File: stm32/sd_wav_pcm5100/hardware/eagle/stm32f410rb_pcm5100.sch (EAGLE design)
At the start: 33 parts, among them IC1 STM32F410_8_B_LQFP64, U5 PCM5100

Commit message: added dirtypcb gerbers
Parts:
- C28, C29: value 2200pF -> 2.2nF
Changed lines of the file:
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@@
 <grid distance="0.1" unitdist="inch" unit="inch" style="lines" multiple="1" display="no" altdistance="0.01" altunitdist="inch" altunit="inch"/>
 <layers>
-<layer number="1" name="Top" color="4" fill="1" visible="yes" active="no"/>
-<layer number="2" name="Route2" color="1" fill="3" visible="yes" active="no"/>
-<layer number="3" name="Route3" color="4" fill="3" visible="yes" active="no"/>
-<layer number="4" name="Route4" color="1" fill="4" visible="yes" active="no"/>
-<layer number="5" name="Route5" color="4" fill="4" visible="yes" active="no"/>
-<layer number="6" name="Route6" color="1" fill="8" visible="yes" active="no"/>
-<layer number="7" name="Route7" color="4" fill="8" visible="yes" active="no"/>
-<layer number="8" name="Route8" color="1" fill="2" visible="yes" active="no"/>
-<layer number="9" name="Route9" color="4" fill="2" visible="yes" active="no"/>
-<layer number="10" name="Route10" color="1" fill="7" visible="yes" active="no"/>
-<layer number="11" name="Route11" color="4" fill="7" visible="yes" active="no"/>
-<layer number="12" name="Route12" color="1" fill="5" visible="yes" active="no"/>
-<layer number="13" name="Route13" color="4" fill="5" visible="yes" active="no"/>
-<layer number="14" name="Route14" color="1" fill="6" visible="yes" active="no"/>
-<layer number="15" name="Route15" color="4" fill="6" visible="yes" active="no"/>
-<layer number="16" name="Bottom" color="1" fill="1" visible="yes" active="no"/>
-<layer number="17" name="Pads" color="2" fill="1" visible="yes" active="no"/>
-<layer number="18" name="Vias" color="2" fill="1" visible="yes" active="no"/>
-<layer number="19" name="Unrouted" color="6" fill="1" visible="yes" active="no"/>
-<layer number="20" name="Dimension" color="15" fill="1" visible="yes" active="no"/>
-<layer number="21" name="tPlace" color="7" fill="1" visible="yes" active="no"/>
-<layer number="22" name="bPlace" color="7" fill="1" visible="yes" active="no"/>
-<layer number="23" name="tOrigins" color="15" fill="1" visible="yes" active="no"/>
-<layer number="24" name="bOrigins" color="15" fill="1" visible="yes" active="no"/>
-<layer number="25" name="tNames" color="7" fill="1" visible="yes" active="no"/>
-<layer number="26" name="bNames" color="7" fill="1" visible="yes" active="no"/>
-<layer number="27" name="tValues" color="7" fill="1" visible="yes" active="no"/>
-<layer number="28" name="bValues" color="7" fill="1" visible="yes" active="no"/>
+<layer number="1" name="Top" color="4" fill="1" visible="no" active="no"/>
+<layer number="2" name="Route2" color="1" fill="3" visible="no" active="no"/>
+<layer number="3" name="Route3" color="4" fill="3" visible="no" active="no"/>
+<layer number="4" name="Route4" color="1" fill="4" visible="no" active="no"/>
+<layer number="5" name="Route5" color="4" fill="4" visible="no" active="no"/>
+<layer number="6" name="Route6" color="1" fill="8" visible="no" active="no"/>
+<layer number="7" name="Route7" color="4" fill="8" visible="no" active="no"/>
+<layer number="8" name="Route8" color="1" fill="2" visible="no" active="no"/>
+<layer number="9" name="Route9" color="4" fill="2" visible="no" active="no"/>
+<layer number="10" name="Route10" color="1" fill="7" visible="no" active="no"/>
+<layer number="11" name="Route11" color="4" fill="7" visible="no" active="no"/>
+<layer number="12" name="Route12" color="1" fill="5" visible="no" active="no"/>
+<layer number="13" name="Route13" color="4" fill="5" visible="no" active="no"/>
+<layer number="14" name="Route14" color="1" fill="6" visible="no" active="no"/>
+<layer number="15" name="Route15" color="4" fill="6" visible="no" active="no"/>
+<layer number="16" name="Bottom" color="1" fill="1" visible="no" active="no"/>
+<layer number="17" name="Pads" color="2" fill="1" visible="no" active="no"/>
+<layer number="18" name="Vias" color="2" fill="1" visible="no" active="no"/>
+<layer number="19" name="Unrouted" color="6" fill="1" visible="no" active="no"/>
+<layer number="20" name="Dimension" color="15" fill="1" visible="no" active="no"/>
+<layer number="21" name="tPlace" color="7" fill="1" visible="no" active="no"/>
+<layer number="22" name="bPlace" color="7" fill="1" visible="no" active="no"/>
+<layer number="23" name="tOrigins" color="15" fill="1" visible="no" active="no"/>
+<layer number="24" name="bOrigins" color="15" fill="1" visible="no" active="no"/>
+<layer number="25" name="tNames" color="7" fill="1" visible="no" active="no"/>
+<layer number="26" name="bNames" color="7" fill="1" visible="no" active="no"/>
+<layer number="27" name="tValues" color="7" fill="1" visible="no" active="no"/>
+<layer number="28" name="bValues" color="7" fill="1" visible="no" active="no"/>
 <layer number="29" name="tStop" color="7" fill="3" visible="no" active="no"/>
 <layer number="30" name="bStop" color="7" fill="6" visible="no" active="no"/>
@@
 <layer number="35" name="tGlue" color="7" fill="4" visible="no" active="no"/>
 <layer number="36" name="bGlue" color="7" fill="5" visible="no" active="no"/>
-<layer number="37" name="tTest" color="7" fill="1" visible="yes" active="no"/>
-<layer number="38" name="bTest" color="7" fill="1" visible="yes" active="no"/>
+<layer number="37" name="tTest" color="7" fill="1" visible="no" active="no"/>
+<layer number="38" name="bTest" color="7" fill="1" visible="no" active="no"/>
 <layer number="39" name="tKeepout" color="4" fill="11" visible="no" active="no"/>
 <layer number="40" name="bKeepout" color="1" fill="11" visible="no" active="no"/>
@@
 <layer number="44" name="Drills" color="7" fill="1" visible="no" active="no"/>
 <layer number="45" name="Holes" color="7" fill="1" visible="no" active="no"/>
-<layer number="46" name="Milling" color="3" fill="1" visible="yes" active="no"/>
-<layer number="47" name="Measures" color="7" fill="1" visible="yes" active="no"/>
-<layer number="48" name="Document" color="7" fill="1" visible="yes" active="no"/>
-<layer number="49" name="Reference" color="7" fill="1" visible="yes" active="no"/>
-<layer number="50" name="dxf" color="7" fill="1" visible="yes" active="no"/>
-<layer number="51" name="tDocu" color="7" fill="1" visible="yes" active="no"/>
-<layer number="52" name="bDocu" color="7" fill="1" visible="yes" active="no"/>
-<layer number="53" name="tGND_GNDA" color="7" fill="9" visible="yes" active="no"/>
-<layer number="54" name="bGND_GNDA" color="1" fill="9" visible="yes" active="no"/>
-<layer number="56" name="wert" color="7" fill="1" visible="yes" active="no"/>
-<layer number="57" name="tCAD" color="7" fill="1" visible="yes" active="no"/>
-<layer number="59" name="tCarbon" color="7" fill="1" visible="yes" active="no"/>
-<layer number="60" name="bCarbon" color="7" fill="1" visible="yes" active="no"/>
+<layer number="46" name="Milling" color="3" fill="1" visible="no" active="no"/>
+<layer number="47" name="Measures" color="7" fill="1" visible="no" active="no"/>
+<layer number="48" name="Document" color="7" fill="1" visible="no" active="no"/>
+<layer number="49" name="Reference" color="7" fill="1" visible="no" active="no"/>
+<layer number="50" name="dxf" color="7" fill="1" visible="no" active="no"/>
+<layer number="51" name="tDocu" color="7" fill="1" visible="no" active="no"/>
+<layer number="52" name="bDocu" color="7" fill="1" visible="no" active="no"/>
+<layer number="53" name="tGND_GNDA" color="7" fill="9" visible="no" active="no"/>
+<layer number="54" name="bGND_GNDA" color="1" fill="9" visible="no" active="no"/>
+<layer number="56" name="wert" color="7" fill="1" visible="no" active="no"/>
+<layer number="57" name="tCAD" color="7" fill="1" visible="no" active="no"/>
+<layer number="59" name="tCarbon" color="7" fill="1" visible="no" active="no"/>
+<layer number="60" name="bCarbon" color="7" fill="1" visible="no" active="no"/>
 <layer number="90" name="Modules" color="5" fill="1" visible="yes" active="yes"/>
 <layer number="91" name="Nets" color="2" fill="1" visible="yes" active="yes"/>
@@
 <part name="C26" library="SparkFun-Passives" deviceset="CAP" device="0805" value="0.1uF"/>
 <part name="C27" library="SparkFun-Passives" deviceset="CAP" device="0805" value="10uF"/>
-<part name="C28" library="SparkFun-Passives" deviceset="CAP" device="0805" value="2200pF"/>
-<part name="C29" library="SparkFun-Passives" deviceset="CAP" device="0805" value="2200pF"/>
+<part name="C28" library="SparkFun-Passives" deviceset="CAP" device="0805" value="2.2nF"/>
+<part name="C29" library="SparkFun-Passives" deviceset="CAP" device="0805" value="2.2nF"/>
 <part name="R6" library="SparkFun-Passives" deviceset="RESISTOR" device="0805-RES" value="470"/>
 <part name="R7" library="SparkFun-Passives" deviceset="RESISTOR" device="0805-RES" value="470"/>

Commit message: refactored pcb
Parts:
- JP2: value M023.5MM -> Vsupply - 3.3Vcc
- MMC1: value MICROSD_AMPHENOL -> Amphenol
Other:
- note added: "TT"
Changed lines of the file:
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@@
 <setting verticaltext="up"/>
 </settings>
-<grid distance="0.1" unitdist="inch" unit="inch" style="lines" multiple="1" display="no" altdistance="0.01" altunitdist="inch" altunit="inch"/>
+<grid distance="0.01" unitdist="inch" unit="inch" style="dots" multiple="1" display="yes" altdistance="0.01" altunitdist="inch" altunit="inch"/>
 <layers>
 <layer number="1" name="Top" color="4" fill="1" visible="no" active="no"/>
@@
 <part name="C9" library="SparkFun-Passives" deviceset="CAP" device="0805" value="0.1uF"/>
 <part name="GND14" library="supply1" deviceset="GND" device=""/>
-<part name="MMC1" library="microsd_amphenol" deviceset="MICROSD_AMPHENOL" device=""/>
+<part name="MMC1" library="microsd_amphenol" deviceset="MICROSD_AMPHENOL" device="" value="Amphenol"/>
 <part name="P+6" library="supply1" deviceset="VCC" device="" value="+3V3"/>
 <part name="P+1" library="supply1" deviceset="VCC" device="" value="+3V3"/>
@@
 <part name="JP6" library="SparkFun-Connectors" deviceset="M04" device="SCREW" value="AUDIO_OUT"/>
 <part name="IC1" library="pel_stm32" deviceset="STM32F410_8_B_LQFP64" device=""/>
-<part name="JP2" library="SparkFun-Connectors" deviceset="M02" device="3.5MM"/>
+<part name="JP2" library="SparkFun-Connectors" deviceset="M02" device="3.5MM" value="Vsupply - 3.3Vcc"/>
 <part name="P+4" library="supply1" deviceset="VCC" device="" value="+3V3"/>
 <part name="GND10" library="supply1" deviceset="GND" device=""/>
@@
 <sheet>
 <plain>
+<rectangle x1="233.172" y1="22.606" x2="234.442" y2="22.86" layer="94"/>
+<rectangle x1="233.172" y1="22.098" x2="234.442" y2="22.352" layer="94"/>
+<rectangle x1="233.172" y1="21.59" x2="234.442" y2="21.844" layer="94"/>
+<rectangle x1="235.712" y1="22.606" x2="236.982" y2="22.86" layer="94"/>
+<rectangle x1="235.712" y1="22.098" x2="236.982" y2="22.352" layer="94"/>
+<rectangle x1="235.712" y1="21.59" x2="236.982" y2="21.844" layer="94"/>
+<rectangle x1="234.188" y1="22.098" x2="235.458" y2="22.352" layer="94" rot="R90"/>
+<rectangle x1="234.696" y1="22.098" x2="235.966" y2="22.352" layer="94" rot="R90"/>
+<rectangle x1="232.664" y1="23.114" x2="237.49" y2="23.368" layer="94"/>
+<rectangle x1="232.664" y1="19.812" x2="237.49" y2="20.066" layer="94"/>
+<text x="234.188" y="20.32" size="1.016" layer="94" ratio="20">TT</text>
+<rectangle x1="237.236" y1="20.066" x2="237.49" y2="23.114" layer="94"/>
+<rectangle x1="232.664" y1="20.066" x2="232.918" y2="23.114" layer="94"/>
 </plain>
 <instances>
@@
 </instance>
 <instance part="GND14" gate="1" x="74.422" y="126.746" rot="R270"/>
-<instance part="MMC1" gate="G$1" x="138.43" y="131.826" smashed="yes"/>
+<instance part="MMC1" gate="G$1" x="138.43" y="131.826" smashed="yes">
+<attribute name="NAME" x="148.59" y="159.766" size="1.778" layer="95"/>
+<attribute name="VALUE" x="151.13" y="157.226" size="1.778" layer="95"/>
+</instance>
 <instance part="P+6" gate="VCC" x="87.122" y="162.814"/>
 <instance part="P+1" gate="VCC" x="133.604" y="165.1"/>

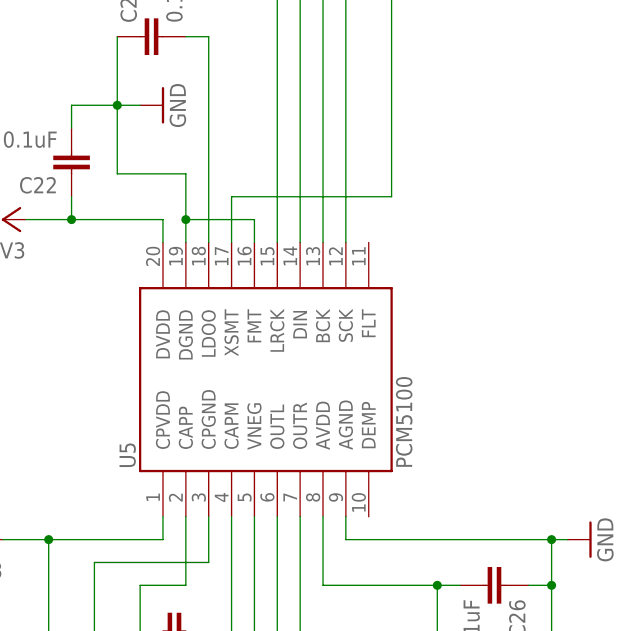
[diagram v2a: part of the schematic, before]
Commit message: added eagle project libs in one file
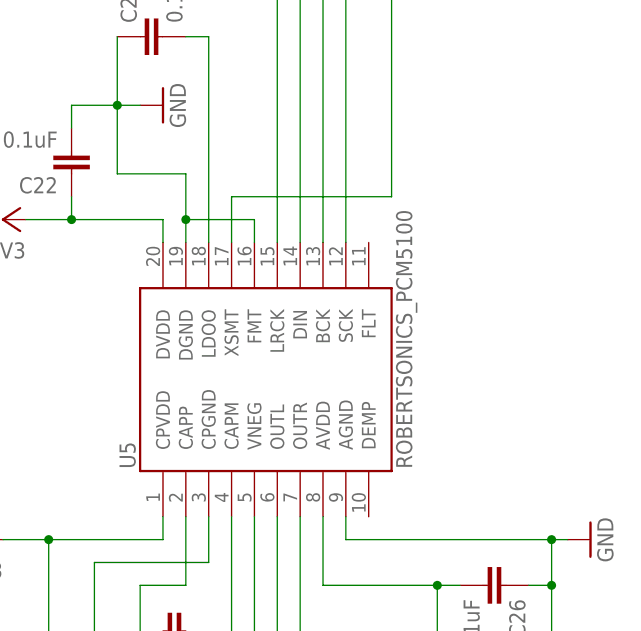
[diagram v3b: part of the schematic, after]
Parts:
- U5: value PCM5100 -> ROBERTSONICS_PCM5100; device robertsonics:PCM5100 -> stm32f410rb_pcm5100:ROBERTSONICS_PCM5100
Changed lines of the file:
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@@
 <setting verticaltext="up"/>
 </settings>
-<grid distance="0.01" unitdist="inch" unit="inch" style="dots" multiple="1" display="yes" altdistance="0.01" altunitdist="inch" altunit="inch"/>
+<grid distance="0.1" unitdist="inch" unit="inch" style="lines" multiple="1" display="no" altdistance="0.01" altunitdist="inch" altunit="inch"/>
 <layers>
 <layer number="1" name="Top" color="4" fill="1" visible="no" active="no"/>
@@
 </classes>
 <parts>
-<part name="U5" library="robertsonics" deviceset="PCM5100" device=""/>
+<part name="U5" library="stm32f410rb_pcm5100" deviceset="ROBERTSONICS_PCM5100" device=""/>
 <part name="C21" library="SparkFun-Passives" deviceset="CAP" device="0805" value="0.1uF"/>
 <part name="C22" library="SparkFun-Passives" deviceset="CAP" device="0805" value="0.1uF"/>

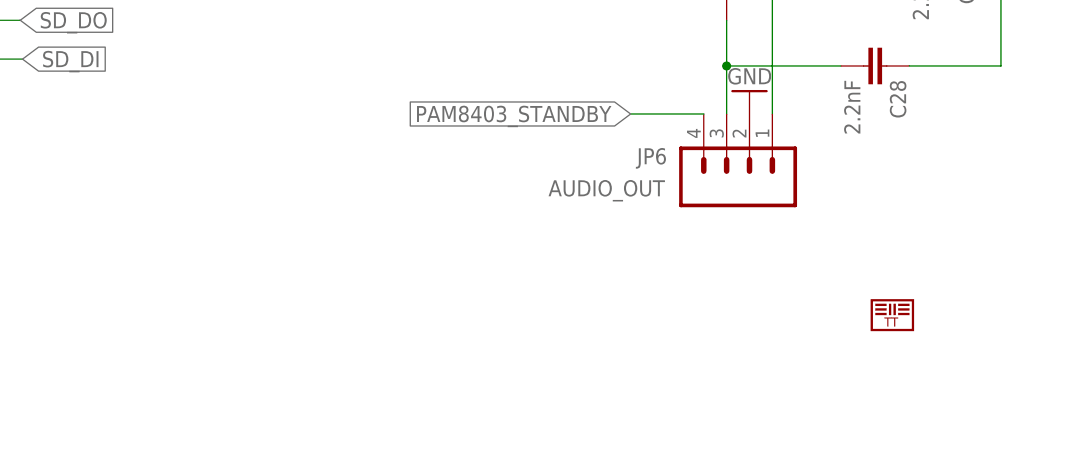
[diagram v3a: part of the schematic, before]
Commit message: updated schematics
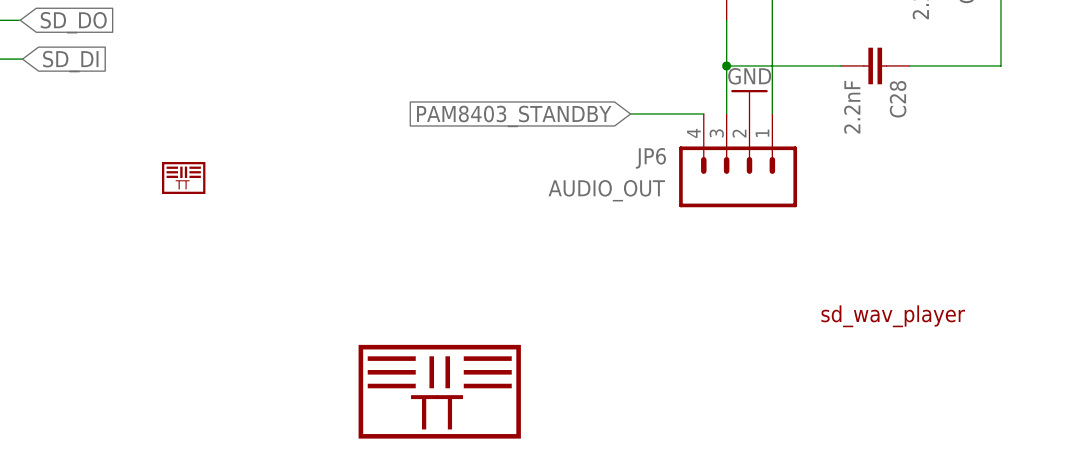
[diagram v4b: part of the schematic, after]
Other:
- note added: "sd_wav_player"
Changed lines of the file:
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@@
 <setting verticaltext="up"/>
 </settings>
-<grid distance="0.1" unitdist="inch" unit="inch" style="lines" multiple="1" display="no" altdistance="0.01" altunitdist="inch" altunit="inch"/>
+<grid distance="0.01" unitdist="inch" unit="inch" style="dots" multiple="1" display="yes" altdistance="0.01" altunitdist="inch" altunit="inch"/>
 <layers>
 <layer number="1" name="Top" color="4" fill="1" visible="no" active="no"/>
@@
 <sheet>
 <plain>
-<rectangle x1="233.172" y1="22.606" x2="234.442" y2="22.86" layer="94"/>
-<rectangle x1="233.172" y1="22.098" x2="234.442" y2="22.352" layer="94"/>
-<rectangle x1="233.172" y1="21.59" x2="234.442" y2="21.844" layer="94"/>
-<rectangle x1="235.712" y1="22.606" x2="236.982" y2="22.86" layer="94"/>
-<rectangle x1="235.712" y1="22.098" x2="236.982" y2="22.352" layer="94"/>
-<rectangle x1="235.712" y1="21.59" x2="236.982" y2="21.844" layer="94"/>
-<rectangle x1="234.188" y1="22.098" x2="235.458" y2="22.352" layer="94" rot="R90"/>
-<rectangle x1="234.696" y1="22.098" x2="235.966" y2="22.352" layer="94" rot="R90"/>
-<rectangle x1="232.664" y1="23.114" x2="237.49" y2="23.368" layer="94"/>
-<rectangle x1="232.664" y1="19.812" x2="237.49" y2="20.066" layer="94"/>
-<text x="234.188" y="20.32" size="1.016" layer="94" ratio="20">TT</text>
-<rectangle x1="237.236" y1="20.066" x2="237.49" y2="23.114" layer="94"/>
-<rectangle x1="232.664" y1="20.066" x2="232.918" y2="23.114" layer="94"/>
+<rectangle x1="154.432" y1="37.846" x2="155.702" y2="38.1" layer="94"/>
+<rectangle x1="154.432" y1="37.338" x2="155.702" y2="37.592" layer="94"/>
+<rectangle x1="154.432" y1="36.83" x2="155.702" y2="37.084" layer="94"/>
+<rectangle x1="156.972" y1="37.846" x2="158.242" y2="38.1" layer="94"/>
+<rectangle x1="156.972" y1="37.338" x2="158.242" y2="37.592" layer="94"/>
+<rectangle x1="156.972" y1="36.83" x2="158.242" y2="37.084" layer="94"/>
+<rectangle x1="155.448" y1="37.338" x2="156.718" y2="37.592" layer="94" rot="R90"/>
+<rectangle x1="155.956" y1="37.338" x2="157.226" y2="37.592" layer="94" rot="R90"/>
+<rectangle x1="153.924" y1="38.354" x2="158.75" y2="38.608" layer="94"/>
+<rectangle x1="153.924" y1="35.052" x2="158.75" y2="35.306" layer="94"/>
+<text x="155.448" y="35.56" size="1.016" layer="94" ratio="20">TT</text>
+<rectangle x1="158.496" y1="35.306" x2="158.75" y2="38.354" layer="94"/>
+<rectangle x1="153.924" y1="35.306" x2="154.178" y2="38.354" layer="94"/>
+<rectangle x1="176.784" y1="16.51" x2="182.118" y2="17.018" layer="94"/>
+<rectangle x1="176.784" y1="14.986" x2="182.118" y2="15.494" layer="94"/>
+<rectangle x1="176.784" y1="13.462" x2="182.118" y2="13.97" layer="94"/>
+<rectangle x1="187.452" y1="16.51" x2="192.786" y2="17.018" layer="94"/>
+<rectangle x1="187.452" y1="14.986" x2="192.786" y2="15.494" layer="94"/>
+<rectangle x1="187.452" y1="13.462" x2="192.786" y2="13.97" layer="94"/>
+<rectangle x1="183.642" y1="13.462" x2="184.15" y2="17.018" layer="94"/>
+<rectangle x1="185.42" y1="13.462" x2="185.928" y2="17.018" layer="94"/>
+<text x="181.61" y="8.89" size="3.81" layer="94" ratio="20">TT</text>
+<rectangle x1="193.294" y1="7.874" x2="193.802" y2="18.288" layer="94"/>
+<rectangle x1="175.768" y1="7.874" x2="176.276" y2="18.288" layer="94"/>
+<rectangle x1="176.276" y1="17.78" x2="193.294" y2="18.288" layer="94"/>
+<rectangle x1="176.276" y1="7.874" x2="193.294" y2="8.382" layer="94"/>
+<text x="227.076" y="20.828" size="1.778" layer="94">sd_wav_player</text>
 </plain>
 <instances>
